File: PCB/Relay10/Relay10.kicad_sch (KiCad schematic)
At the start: 43 parts, among them J1 USB-C, J10 O8, J11 O9, J12 O10, J2 POWER, J3 O1, J4 O2, J5 O3, J6 O4, J7 O5, J8 O6, J9 O7, U1 ESP32-PICO-MINI-02, U10 QR, U2 FT231XQ, U3 ISL89410, U4 ISL89410, U5 ISL89410, U6 ISL89410, U7 ISL89410, U8 LMR16006+FB, U9 AA

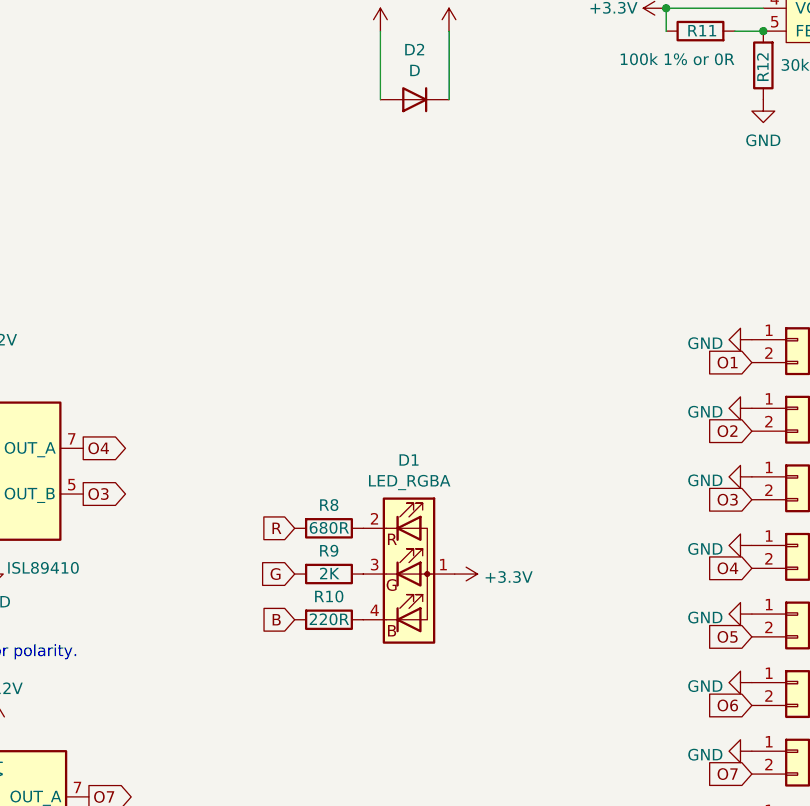
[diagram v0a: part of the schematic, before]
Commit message: Update Relay10 and document
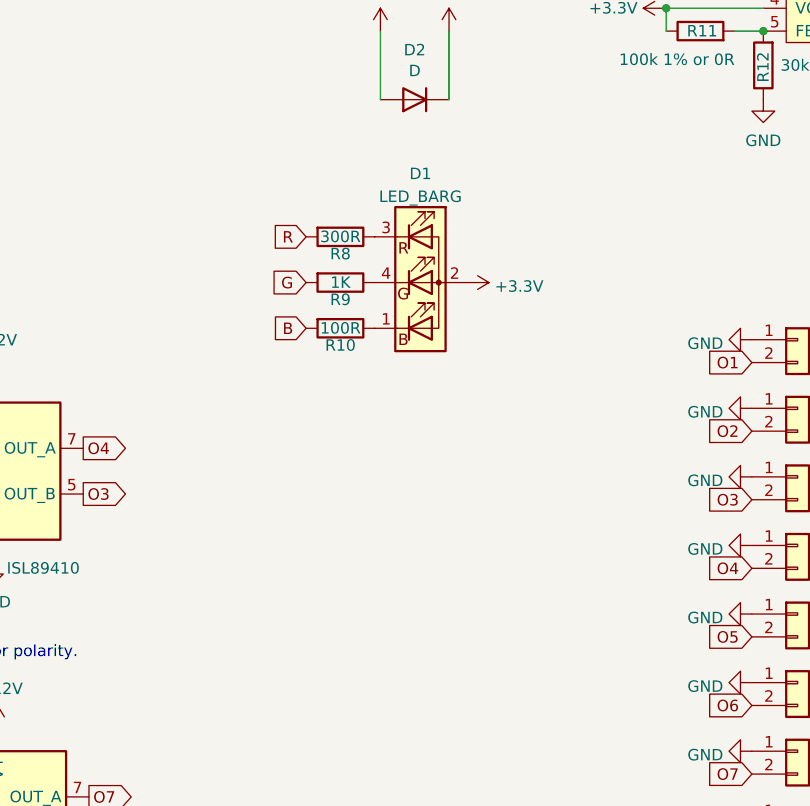
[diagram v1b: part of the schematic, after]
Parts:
- removed D1: LED_RGBA, RevK:LED-RGB-1.6x1.6, symbol Device:LED_ARGB
- added D1: LED_BARG, RevK:MHS190RGBCT, symbol Device:LED_BARG
- J1: footprint RevK:USC16-TR-Round -> RevK:USC16-TR
- J10, J11, J12, J2, J3, J4, J5, J6, J7, J8, J9: footprint RevK:Molex_MiniSPOX_H2RA -> RevK:PTSM-HH1-2-RA
- R10: value 220R -> 100R; Part No (none) -> 0603-220R
- R8: value 680R -> 300R; Part No (none) -> 0603-680R
- R9: value 2K -> 1K; Part No (none) -> 0603-2K
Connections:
- net +3V3: now also D1.2 (A)
- net at R10.1: now also D1.1 (BK)
- net at R8.1: now also D1.3 (RK)
- net at R9.1: now also D1.4 (GK)
